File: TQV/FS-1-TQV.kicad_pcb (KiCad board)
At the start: 2 copper layers, 69.8 x 87.6 mm, 31 parts, among them J1 CAN, J10 XBee_right, J2 Conn_01x03_Male, J4 XBee_left, U1 ISO1050, U2 stm_nucleo_F303K8_fstqv, U3 SparkFun_MPU9250, U4 SparkFun_MPU9250

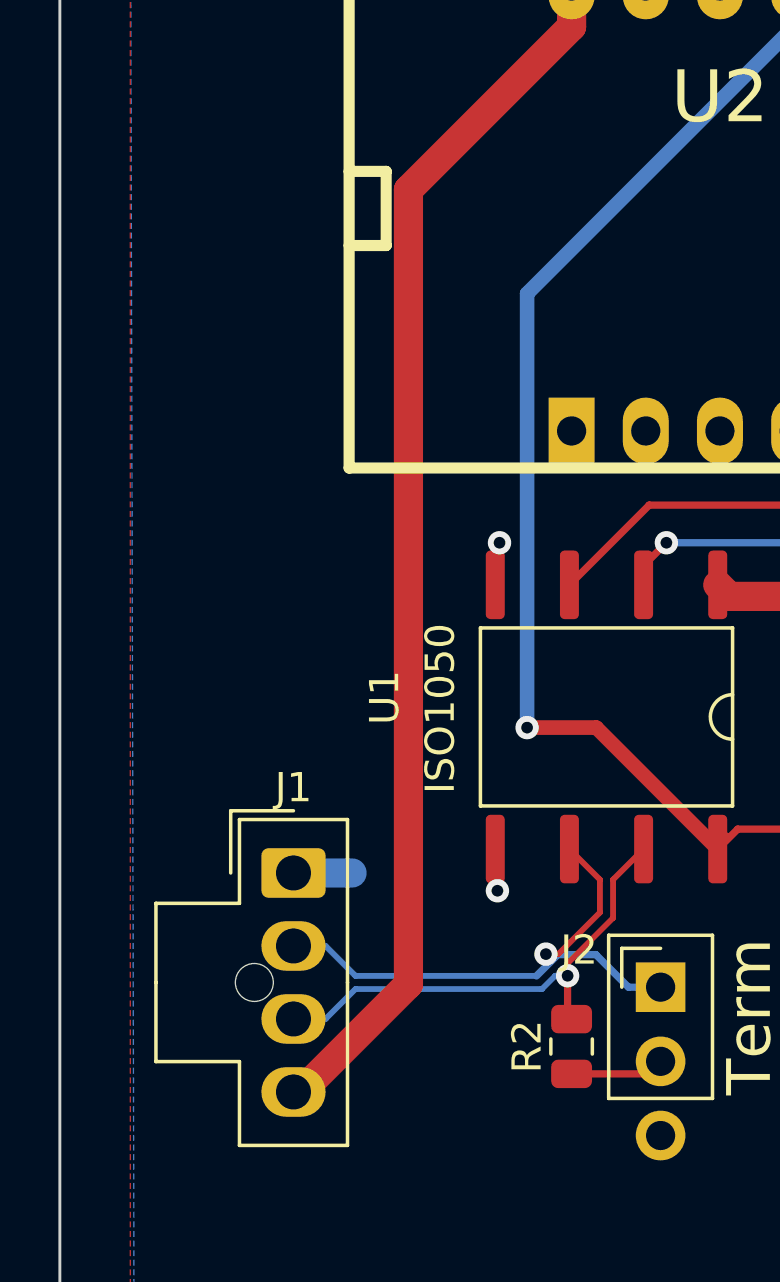
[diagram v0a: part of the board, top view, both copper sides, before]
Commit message: New Molex NanoFit 1x4 footprint that passes DRC ._.
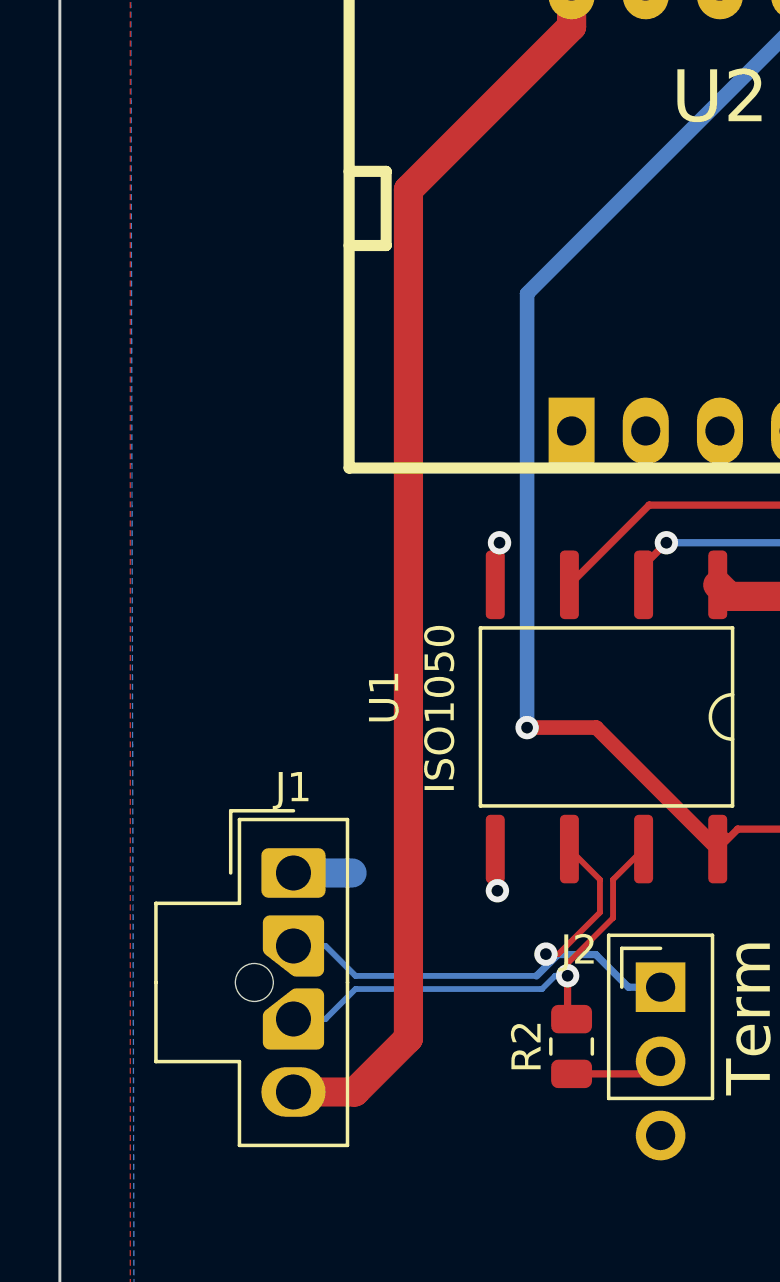
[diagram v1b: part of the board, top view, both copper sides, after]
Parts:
- J1: footprint Connector_Molex:Molex_Nano-Fit_105309-xx04_1x04_P2.50mm_Vertical -> FSFootprints:Molex_Nano-Fit_1x04_P2.50mm_Vertical_Custom_Pads
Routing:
- net Net-(J1-Pad4): track 42.0 -> 43.3 mm
